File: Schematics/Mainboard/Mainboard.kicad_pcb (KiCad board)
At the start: 2 copper layers, 179.6 x 117.9 mm, 70 parts, among them J1 USB-C, J10 CHG in, J11 Batt, J12 CHG out, J13 DC-DC in, J14 DC-DC out, J16 OLED, J18 Power, J19 Power, J2 USB in, J20 I0, J21 Data, J22 Data, J23 I1, J24 I2C OLED 0, J25 I2C OLED 1, J26 I2C OLED 2, J27 I2C OLED 3, J28 I2C OLED 4, J29 I2C OLED 5, J3 USB out, J30 I2C OLED 6, J31 I2C OLED 7, J32 I2, J33 I3, J34 O0, J35 O1, J36 O2, J37 O3, J4 NFC Conn, J5 Prot in, J6 Prot out, J7 Power rail, J8 Power rail, J9 ICSP, Q1 AO3401A, SW1 RESET, U1 ESP32-WROOM-32, U2 TCA9548APWR, U3 ATmega328-AU, Y1 16MHz YSX321SL

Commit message: Added Mainboard rev 1.0
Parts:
- removed J18, J19: Power, Connector_PinSocket_2.54mm:PinSocket_1x03_P2.54mm_Vertical
- removed J21, J22: Data, Connector_PinSocket_2.54mm:PinSocket_1x03_P2.54mm_Vertical
- removed Y1: 16MHz YSX321SL, Crystal:Crystal_SMD_3225-4Pin_3.2x2.5mm
- added C10: 10u, Capacitor_SMD:C_0603_1608Metric, B.Cu at (70.6, 74.4)
- added C9: 10u, Capacitor_SMD:C_0603_1608Metric, B.Cu at (70.6, 57.6)
- added D3: Red, LED_SMD:LED_1206_3216Metric_Castellated, F.Cu at (62.8, 51.8)
- added D5: Gre, LED_SMD:LED_1206_3216Metric_Castellated, F.Cu at (62.8, 54.1)
- added D6: Yel, LED_SMD:LED_1206_3216Metric_Castellated, F.Cu at (62.8, 56.4)
- added H1: MountingHole, MountingHole:MountingHole_3.2mm_M3, F.Cu at (78.1, 45.2)
- added H2: MountingHole, MountingHole:MountingHole_3.2mm_M3, F.Cu at (236.2, 45.2)
- added H3: MountingHole, MountingHole:MountingHole_3.2mm_M3, F.Cu at (63.9, 156.1)
- added H4: MountingHole, MountingHole:MountingHole_3.2mm_M3, F.Cu at (236.2, 156.1)
- added J44: Del in, custom:PinSocket_1x06_P2.54mm_Vertical, B.Cu at (139.7, 73.0)
- added J45: Del out, custom:PinSocket_1x06_P2.54mm_Vertical, B.Cu at (159.5, 73.0)
- added JP3: Jumper, Jumper:SolderJumper-2_P1.3mm_Open_Pad1.0x1.5mm, B.Cu at (149.1, 78.2)
- added JP4: Jumper, Jumper:SolderJumper-2_P1.3mm_Open_Pad1.0x1.5mm, B.Cu at (149.1, 80.8)
- added JP5: SHDN, Jumper:SolderJumper-2_P1.3mm_Open_Pad1.0x1.5mm, F.Cu at (70.4, 91.4)
- added JP6: DC_DC, Jumper:SolderJumper-2_P1.3mm_Open_Pad1.0x1.5mm, F.Cu at (86.4, 89.4)
- added Q2: DTC143T, Package_TO_SOT_SMD:SOT-323_SC-70, B.Cu at (101.6, 56.9)
- added Q3: DTC143T, Package_TO_SOT_SMD:SOT-323_SC-70, B.Cu at (101.6, 49.0)
- added R17: 47k, Resistor_SMD:R_0603_1608Metric, B.Cu at (121.4, 55.9)
- added R18: 47k, Resistor_SMD:R_0603_1608Metric, B.Cu at (185.4, 55.9)
- added R19: 47k, Resistor_SMD:R_0603_1608Metric, B.Cu at (114.3, 50.8)
- added R20: 1k5, Resistor_SMD:R_0603_1608Metric, B.Cu at (74.2, 60.9)
- added R21: 1k5, Resistor_SMD:R_0603_1608Metric, B.Cu at (75.7, 60.9)
- added R22: 1k5, Resistor_SMD:R_0603_1608Metric, B.Cu at (77.2, 60.9)
- added R23: 1k, Resistor_SMD:R_0603_1608Metric, B.Cu at (75.7, 71.1)
- added R24: 1k, Resistor_SMD:R_0603_1608Metric, B.Cu at (75.7, 74.4)
- added R25: 10k, Resistor_SMD:R_0603_1608Metric, B.Cu at (74.2, 71.1)
- added R26: 10k, Resistor_SMD:R_0603_1608Metric, B.Cu at (74.2, 74.4)
- added R31: 5k1, Resistor_SMD:R_0603_1608Metric, F.Cu at (66.8, 47.6)
- added R32: 5k1, Resistor_SMD:R_0603_1608Metric, F.Cu at (69.8, 47.6)
- added R6: 0, Resistor_SMD:R_1206_3216Metric, B.Cu at (101.1, 54.1)
- added R7: 0, Resistor_SMD:R_1206_3216Metric, B.Cu at (101.1, 51.6)
- added SW2: SW_SPDT, custom:SW-TH_SS-12D11G5, B.Cu at (72.6, 123.4)
- added SW3: Rot, Rotary_Encoder:RotaryEncoder_Alps_EC11E-Switch_Vertical_H20mm, F.Cu at (174.6, 50.9)
- added SW4: Rot, Rotary_Encoder:RotaryEncoder_Alps_EC11E-Switch_Vertical_H20mm, F.Cu at (125.1, 55.8)
- added U4: PCF8574TS, Package_SO:SSOP-20_4.4x6.5mm_P0.65mm, B.Cu at (149.4, 94.3)
- added U5: MCP73833, Package_SO:MSOP-10_3x3mm_P0.5mm, B.Cu at (73.7, 66.0)
- C5: value 0u1 -> 10u
- C7, C8: value 12p -> 10u
- D1: footprint LED_SMD:LED_0603_1608Metric -> LED_SMD:LED_1206_3216Metric_Castellated
- D2, Q1, R5: moved to B.Cu
- D4: footprint LED_SMD:LED_SK6805_PLCC4_2.4x2.7mm_P1.3mm -> LED_THT:LED_BL-FL7680RGB
- J11: footprint Connector_JST:JST_PH_S2B-PH-K_1x02_P2.00mm_Horizontal -> Connector_JST:JST_PH_S2B-PH-SM4-TB_1x02-1MP_P2.00mm_Horizontal
- J16, J24, J25, J26, J27, J28, J29, J30, J31: footprint Connector_PinHeader_2.54mm:PinHeader_1x04_P2.54mm_Vertical_SMD_Pin1Left -> Connector_PinSocket_2.54mm:PinSocket_1x04_P2.54mm_Vertical
- J2: value USB in -> Pololu DC-DC; footprint custom:PinSocket_1x06_P2.54mm_Vertical -> Connector_PinSocket_2.54mm:PinSocket_1x04_P2.54mm_Vertical
- J3: value USB out -> USB Alt; footprint custom:PinSocket_1x06_P2.54mm_Vertical -> Connector_PinSocket_2.54mm:PinSocket_1x04_P2.54mm_Vertical; moved to F.Cu
- J9: value ICSP -> Batt alt; footprint Connector_PinSocket_2.54mm:PinSocket_2x03_P2.54mm_Vertical -> Connector_PinSocket_2.54mm:PinSocket_1x02_P2.54mm_Vertical; moved to B.Cu
- JP1, JP2: footprint Jumper:SolderJumper-2_P1.3mm_Bridged_Pad1.0x1.5mm -> Jumper:SolderJumper-2_P1.3mm_Open_Pad1.0x1.5mm
- R1, R12, R14, R15, R2, R3: value 10K -> 10k
- R11, R13: value 1K -> 47k
- R16: value 10K -> 47k; moved to B.Cu
- U3: value ATmega328-AU -> CH340B; footprint Package_QFP:TQFP-32_7x7mm_P0.8mm -> Package_SO:SOIC-16_3.9x9.9mm_P1.27mm
- moved U3 64.3 mm to (92.1, 50.3), turned to 0 degrees
- moved C6 58.6 mm to (88.6, 57.8), turned to 0 degrees
- moved C5 58.3 mm to (88.6, 56.3), turned to 0 degrees
- moved J2 55.7 mm to (67.1, 96.5), turned to 0 degrees
- moved C8 52.5 mm to (114.3, 55.9), turned to 180 degrees
- moved R16 51.8 mm to (178.3, 50.8), turned to 0 degrees
- moved J9 49.4 mm to (89.4, 65.0)
- moved C7 41.2 mm to (185.4, 50.8)
- moved R13 37.2 mm to (121.4, 50.8), turned to 180 degrees
- moved R11 32.6 mm to (178.3, 55.9), turned to 0 degrees
- moved J4 26.6 mm to (198.6, 45.5), turned to 180 degrees
- moved J3 23.7 mm to (100.1, 44.2), turned to 90 degrees
- moved R15 13.6 mm to (145.1, 110.2), turned to 0 degrees
- moved R12 13.3 mm to (155.2, 111.0), turned to -90 degrees
- moved R14 11.9 mm to (153.7, 111.0), turned to -90 degrees
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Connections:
- C6 pad 1: GND -> +3V3
- C6 pad 2: Net-(C6-Pad2) -> GND
- C7 pad 1: GND -> +3V3
- C7 pad 2: /User interface/XTAL1 -> GND
- C8 pad 1: /User interface/XTAL2 -> +3V3
- D4 pad 1: (no net) -> Net-(D4-Pad1)
- D4 pad 4: Net-(D4-Pad4) -> +3V3
- J1 pad A5: (no net) -> Net-(J1-PadA5)
- J1 pad B5: (no net) -> Net-(J1-PadB5)
- J13 pad 2: +BATT -> /Power management/POWER_SW
- J13 pad 3: +BATT -> /Power management/POWER_SW
- J14 pad 2: +3V3 -> /Power management/DCDC
- J14 pad 3: +3V3 -> /Power management/DCDC
- J2 pad 1: (no net) -> /Power management/DCDC
- J2 pad 2: +3V3 -> GND
- J2 pad 3: /USB D+ -> /Power management/POWER_SW
- J2 pad 4: /USB D- -> Net-(J2-Pad4)
- J3 pad 1: (no net) -> /IO0
- J3 pad 2: /TTL TX -> /EN
- J3 pad 4: /IO0 -> /TTL TX
- J34 pad 1: Net-(U3-Pad14) -> Net-(J34-Pad1)
- J35 pad 1: Net-(U3-Pad13) -> Net-(J35-Pad1)
- J36 pad 1: Net-(U3-Pad12) -> Net-(J36-Pad1)
- J37 pad 1: Net-(U3-Pad11) -> Net-(J37-Pad1)
- J4 pad 7: (no net) -> /PN532 IRQ
- J9 pad 1: /User interface/ICSP MISO -> GND
- J9 pad 2: +3V3 -> +BATT
- R10 pad 1: Net-(D4-Pad4) -> Net-(D4-Pad2)
- R11 pad 1: Net-(R11-Pad1) -> /T_B
- R11 pad 2: (no net) -> +3V3
- R12 pad 1: /MUX SCL -> /User interface/OLED SCL
- R13 pad 1: Net-(R13-Pad1) -> /Q_B
- R13 pad 2: (no net) -> +3V3
- R14 pad 1: /MUX SDA -> /User interface/OLED SDA
- R16 pad 1: /User interface/ICSP RST -> /T_A
- R8 pad 1: Net-(D4-Pad2) -> Net-(D4-Pad1)
- U1 pad 13: /RGB R -> /RGB B
- U1 pad 14: /RGB B -> /RGB R
- U1 pad 17: (no net) -> /PN532 IRQ
- U1 pad 8: /T_SW -> /T_B
- U1 pad 9: /T_B -> /T_SW
- U2 pad 22: /MUX SCL -> /User interface/OLED SCL
- U2 pad 23: /MUX SDA -> /User interface/OLED SDA
- U3 pad 1: Net-(J20-Pad1) -> GND
- U3 pad 10: Net-(J33-Pad1) -> (no net)
- U3 pad 11: Net-(U3-Pad11) -> (no net)
- U3 pad 12: Net-(U3-Pad12) -> (no net)
- U3 pad 13: Net-(U3-Pad13) -> /USB-TTL/~{DTR}
- U3 pad 14: Net-(U3-Pad14) -> /USB-TTL/~{RTS}
- U3 pad 15: /User interface/ICSP MOSI -> (no net)
- U3 pad 16: /User interface/ICSP MISO -> +3V3
- U3 pad 2: Net-(J23-Pad1) -> Net-(R6-Pad1)
- U3 pad 3: GND -> Net-(R7-Pad1)
- U3 pad 5: GND -> /USB D+
- U3 pad 6: +3V3 -> /USB D-
- U3 pad 7: /User interface/XTAL1 -> (no net)
- U3 pad 8: /User interface/XTAL2 -> (no net)
- U3 pad 9: Net-(J32-Pad1) -> (no net)
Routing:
- net +3V3: track 199.8 -> 610.0 mm, vias 1 -> 12
- net GND: track 193.7 -> 465.7 mm, vias 2 -> 50
- net Net-(U3-Pad11): track 111.5 -> 0.00 mm, vias 1 -> 0
- net +BATT: track 14.5 -> 108.3 mm, vias 2 -> 0
- net Net-(J37-Pad1): track 0.00 -> 93.5 mm, vias 0 -> 1
- net Net-(U3-Pad12): track 84.7 -> 0.00 mm, vias 1 -> 0
- net /PN532 SCK: track 0.00 -> 78.2 mm, vias 0 -> 1
- net Net-(U3-Pad13): track 76.9 -> 0.00 mm, vias 2 -> 0
- net Net-(J36-Pad1): track 0.00 -> 76.4 mm, vias 0 -> 1
- net Net-(J34-Pad1): track 0.00 -> 75.6 mm, vias 0 -> 1
- net /PN532 MISO: track 0.00 -> 73.9 mm, vias 0 -> 1
- net /PN532 SS: track 0.00 -> 71.1 mm, vias 0 -> 1
- net Net-(U3-Pad14): track 69.3 -> 0.00 mm, vias 1 -> 0
- net Net-(J35-Pad1): track 0.00 -> 67.1 mm, vias 0 -> 1
- net /Power rails/GND Prot: track 197.3 -> 263.5 mm, vias 0 -> 1
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- added copper zone on B.Cu, net +BATT
- added copper zone on B.Cu, net GND
- added copper zone on F.Cu, net GND
- added copper zone on B.Cu, net VBUS
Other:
- board size 179.6 x 117.9 mm -> 179.6 x 118.1 mm

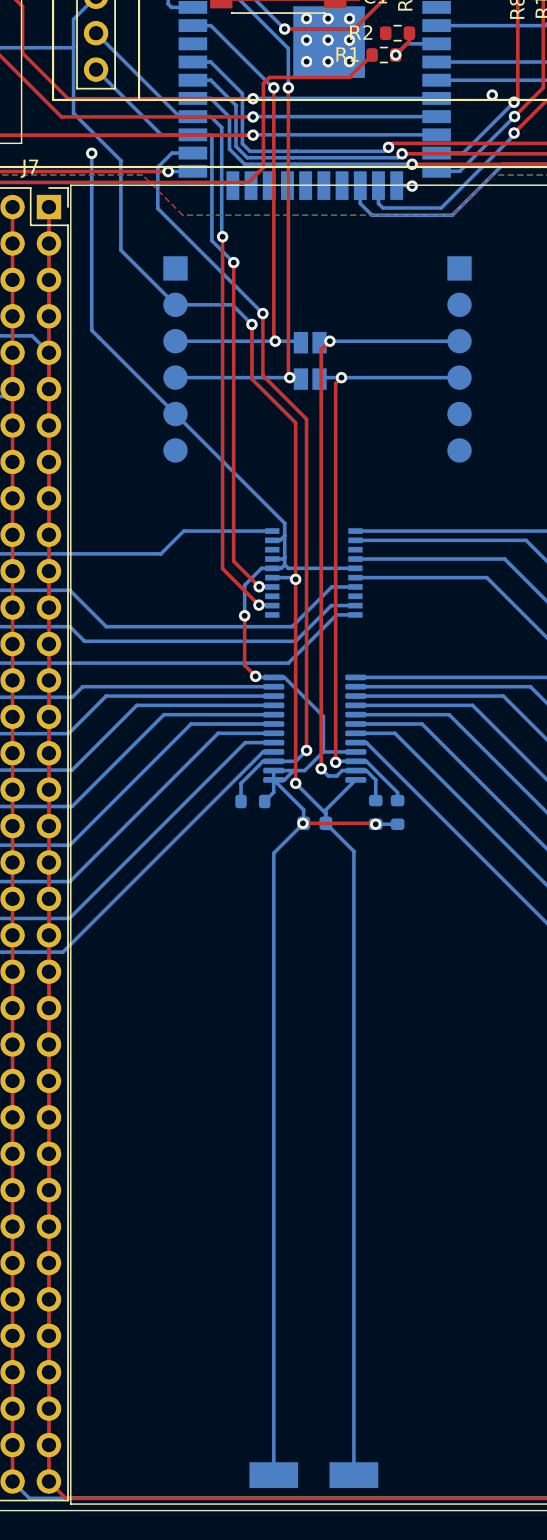
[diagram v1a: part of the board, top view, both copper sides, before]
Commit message: Updated I2C power
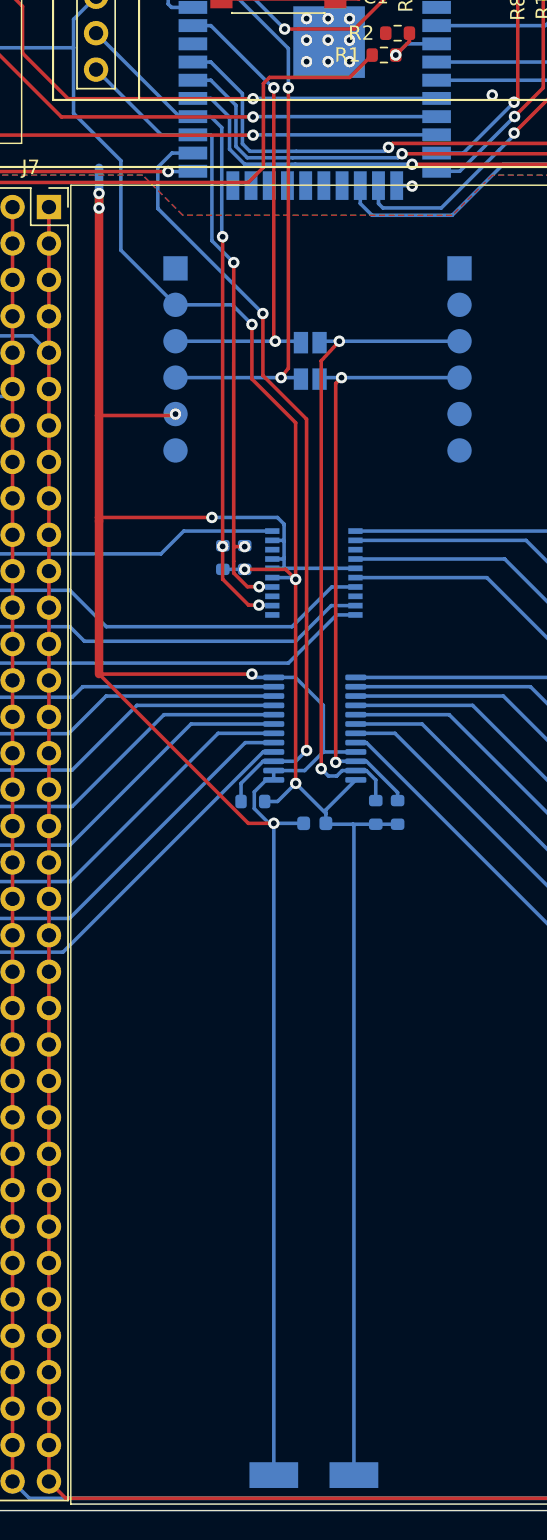
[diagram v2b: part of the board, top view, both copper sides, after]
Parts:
- added R27: 10k, Resistor_SMD:R_0603_1608Metric, B.Cu at (144.5, 93.2)
- added R28: 10k, Resistor_SMD:R_0603_1608Metric, B.Cu at (143.0, 93.2)
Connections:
- R12 pad 2: GND -> +3V3
- R14 pad 2: GND -> +3V3
- R15 pad 2: GND -> +3V3
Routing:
- net GND: track 465.7 -> 499.6 mm, vias 50 -> 51
- net +3V3: track 610.0 -> 622.3 mm, vias 12 -> 13
- net /ALT SDA: track 43.7 -> 45.0 mm, vias 2 -> 3
- net /ALT SCL: track 46.8 -> 47.2 mm, vias 2 -> 3

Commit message: Final print version mainboard
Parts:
- C7, C8: value 10u -> 1u
- R18, R19: value 47k -> 10k
- moved C7 2.43 mm to (186.2, 53.1), turned to 90 degrees
- moved C8 2.43 mm to (113.5, 53.6), turned to -90 degrees
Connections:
- C7 pad 1: +3V3 -> /T_SW
- C8 pad 1: +3V3 -> /Q_SW
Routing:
- net GND: track 499.6 -> 503.6 mm
- net /T_SW: track 35.6 -> 37.6 mm
- net /Q_SW: track 55.5 -> 57.5 mm
